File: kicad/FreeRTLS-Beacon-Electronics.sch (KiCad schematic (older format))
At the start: 28 parts, among them J1 USB_B_Micro, J2 TC2030, U1 STM32F072CBTx, U2 AZ1117IH-3.3TRG1, U3 DWM1001

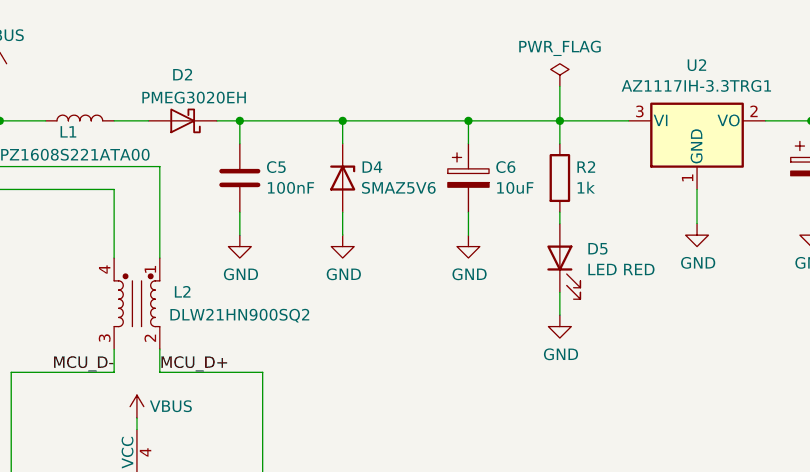
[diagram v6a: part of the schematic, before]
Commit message: Assign footprints
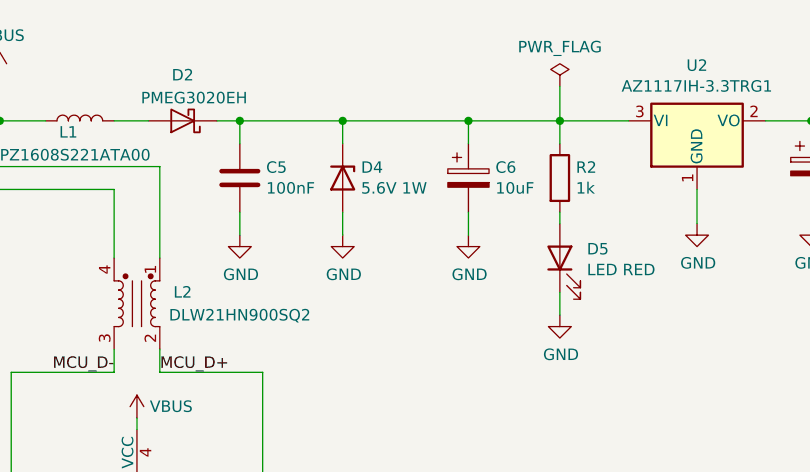
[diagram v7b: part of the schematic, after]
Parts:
- C1, C2, C3, C4, C5, C6, C7, C8, C9: footprint (none) -> Capacitor_SMD:C_0603_1608Metric
- D3: footprint (none) -> LED_SMD:LED_0603_1608Metric
- D4: value SMAZ5V6 -> 5.6V 1W; footprint (none) -> Diode_SMD:D_SOD-123; DK_Detail_Page https://www.digikey.com/en/products/detail/micro-commercial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 -> https://www.digikey.com/en/products/detail/rohm-semiconduct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; Digi-Key_PN SMAZ5V6-TPMSCT-ND -> KDZVTFTR5.6BCT-ND; MPN SMAZ5V6-TP -> KDZVTFTR5.6B; Manufacturer Micro Commercial Co -> Rohm Semiconductor
- D5: footprint (none) -> LED_SMD:LED_0603_1608Metric_Castellated
- D6: footprint (none) -> FreeRTLS-Beacon:LED_L955QEQGC-TR_3.2x2.7mm_P1.7mm
- L1, L3, L4: footprint (none) -> Inductor_SMD:L_0603_1608Metric
- L2: footprint (none) -> FreeRTLS-Beacon:FIL_DLW21HN900SQ2L
- R1, R2, R3, R5: footprint (none) -> Resistor_SMD:R_0603_1608Metric
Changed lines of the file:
@@
 F 0 "C5" H 2615 1296 50  0000 L CNN
 F 1 "100nF" H 2615 1205 50  0000 L CNN
-F 2 "" H 2538 1100 50  0001 C CNN
+F 2 "Capacitor_SMD:C_0603_1608Metric" H 2538 1100 50  0001 C CNN
 F 3 "~" H 2500 1250 50  0001 C CNN
 F 4 "https://www.digikey.com/en/products/detail/kemet/C0603C104Z3VACTU/411099" H 2500 1250 50  0001 C CNN "DK_Detail_Page"
@@
 P 2950 1250
 F 0 "D4" V 2904 1330 50  0000 L CNN
-F 1 "SMAZ5V6" V 2995 1330 50  0000 L CNN
-F 2 "" H 2950 1250 50  0001 C CNN
+F 1 "5.6V 1W" V 2995 1330 50  0000 L CNN
+F 2 "Diode_SMD:D_SOD-123" H 2950 1250 50  0001 C CNN
 F 3 "~" H 2950 1250 50  0001 C CNN
-F 4 "https://www.digikey.com/en/products/detail/micro-commercial-co/SMAZ5V6-TP/1793259" H 2950 1250 50  0001 C CNN "DK_Detail_Page"
-F 5 "SMAZ5V6-TPMSCT-ND" H 2950 1250 50  0001 C CNN "Digi-Key_PN"
-F 6 "SMAZ5V6-TP" H 2950 1250 50  0001 C CNN "MPN"
-F 7 "Micro Commercial Co" H 2950 1250 50  0001 C CNN "Manufacturer"
+F 4 "https://www.digikey.com/en/products/detail/rohm-semiconductor/KDZVTFTR5-6B/9697270" H 2950 1250 50  0001 C CNN "DK_Detail_Page"
+F 5 "KDZVTFTR5.6BCT-ND" H 2950 1250 50  0001 C CNN "Digi-Key_PN"
+F 6 "KDZVTFTR5.6B" H 2950 1250 50  0001 C CNN "MPN"
+F 7 "Rohm Semiconductor" H 2950 1250 50  0001 C CNN "Manufacturer"
 	1    2950 1250
 	0    1    1    0
@@
 F 0 "C6" H 3618 1296 50  0000 L CNN
 F 1 "10uF" H 3618 1205 50  0000 L CNN
-F 2 "" H 3538 1100 50  0001 C CNN
+F 2 "Capacitor_SMD:C_0603_1608Metric" H 3538 1100 50  0001 C CNN
 F 3 "~" H 3500 1250 50  0001 C CNN
 F 4 "https://www.digikey.com/en/products/detail/venkel/C0603X6S100-106MNP/12332839" H 3500 1250 50  0001 C CNN "DK_Detail_Page"
@@
 F 0 "R2" H 3970 1296 50  0000 L CNN
 F 1 "1k" H 3970 1205 50  0000 L CNN
-F 2 "" V 3830 1250 50  0001 C CNN
+F 2 "Resistor_SMD:R_0603_1608Metric" V 3830 1250 50  0001 C CNN
 F 3 "~" H 3900 1250 50  0001 C CNN
 F 4 "https://www.digikey.com/en/products/detail/yageo/RC0603JR-071KL/726677" H 3900 1250 50  0001 C CNN "DK_Detail_Page"
@@
 F 0 "D5" V 3939 1482 50  0000 R CNN
 F 1 "LED RED" V 3848 1482 50  0000 R CNN
-F 2 "" H 3900 1600 50  0001 C CNN
+F 2 "LED_SMD:LED_0603_1608Metric_Castellated" H 3900 1600 50  0001 C CNN
 F 3 "~" H 3900 1600 50  0001 C CNN
 F 4 "https://www.digikey.com/en/products/detail/w%C3%BCrth-elektronik/150060RS75000/4489901" H 3900 1600 50  0001 C CNN "DK_Detail_Page"
@@
 F 0 "C7" H 5118 1246 50  0000 L CNN
 F 1 "10uF" H 5118 1155 50  0000 L CNN
-F 2 "" H 5038 1050 50  0001 C CNN
+F 2 "Capacitor_SMD:C_0603_1608Metric" H 5038 1050 50  0001 C CNN
 F 3 "~" H 5000 1200 50  0001 C CNN
 F 4 "https://www.digikey.com/en/products/detail/venkel/C0603X6S100-106MNP/12332839" H 5000 1200 50  0001 C CNN "DK_Detail_Page"
@@
 F 0 "L3" V 5550 1000 50  0000 C CNN
 F 1 "MPZ1608S601ATA00" V 5350 800 50  0000 C CNN
-F 2 "" H 5450 1000 50  0001 C CNN
+F 2 "Inductor_SMD:L_0603_1608Metric" H 5450 1000 50  0001 C CNN
 F 3 "~" H 5450 1000 50  0001 C CNN
 F 4 "https://www.digikey.com/en/products/detail/tdk-corporation/MPZ1608S601ATA00/765064" H 5450 1000 50  0001 C CNN "DK_Detail_Page"
@@
 F 0 "C1" H 4450 4200 50  0000 L CNN
 F 1 "1uF" H 4450 4100 50  0000 L CNN
-F 2 "" H 4388 4000 50  0001 C CNN
+F 2 "Capacitor_SMD:C_0603_1608Metric" H 4388 4000 50  0001 C CNN
 F 3 "~" H 4350 4150 50  0001 C CNN
 F 4 "https://www.digikey.com/en/products/detail/samsung-electro-mechanics/CL10A105KP8NNNC/3886840" H 4350 4150 50  0001 C CNN "DK_Detail_Page"
@@
 F 0 "C2" H 4800 4200 50  0000 L CNN
 F 1 "100nF" H 4800 4100 50  0000 L CNN
-F 2 "" H 4738 4000 50  0001 C CNN
+F 2 "Capacitor_SMD:C_0603_1608Metric" H 4738 4000 50  0001 C CNN
 F 3 "~" H 4700 4150 50  0001 C CNN
 F 4 "https://www.digikey.com/en/products/detail/kemet/C0603C104Z3VACTU/411099" H 4700 4150 50  0001 C CNN "DK_Detail_Page"
@@
 F 0 "C3" H 5250 4200 50  0000 L CNN
 F 1 "100nF" H 5250 4100 50  0000 L CNN
-F 2 "" H 5188 4000 50  0001 C CNN
+F 2 "Capacitor_SMD:C_0603_1608Metric" H 5188 4000 50  0001 C CNN
 F 3 "~" H 5150 4150 50  0001 C CNN
 F 4 "https://www.digikey.com/en/products/detail/kemet/C0603C104Z3VACTU/411099" H 5150 4150 50  0001 C CNN "DK_Detail_Page"
@@
 F 0 "C4" H 5700 4200 50  0000 L CNN
 F 1 "100nF" H 5700 4100 50  0000 L CNN
-F 2 "" H 5638 4000 50  0001 C CNN
+F 2 "Capacitor_SMD:C_0603_1608Metric" H 5638 4000 50  0001 C CNN
 F 3 "~" H 5600 4150 50  0001 C CNN
 F 4 "https://www.digikey.com/en/products/detail/kemet/C0603C104Z3VACTU/411099" H 5600 4150 50  0001 C CNN "DK_Detail_Page"
@@
 F 0 "R1" H 2220 5246 50  0000 L CNN
 F 1 "1k" H 2220 5155 50  0000 L CNN
-F 2 "" V 2080 5200 50  0001 C CNN
+F 2 "Resistor_SMD:R_0603_1608Metric" V 2080 5200 50  0001 C CNN
 F 3 "~" H 2150 5200 50  0001 C CNN
 F 4 "https://www.digikey.com/en/products/detail/yageo/RC0603JR-071KL/726677" H 2150 5200 50  0001 C CNN "DK_Detail_Page"
@@
 F 0 "D3" V 2150 5050 50  0000 R CNN
 F 1 "LED GREEN" V 2050 5300 50  0000 R CNN
-F 2 "" H 2150 4850 50  0001 C CNN
+F 2 "LED_SMD:LED_0603_1608Metric" H 2150 4850 50  0001 C CNN
 F 3 "~" H 2150 4850 50  0001 C CNN
 F 4 "https://www.digikey.com/en/products/detail/w%C3%BCrth-elektronik/150060GS75000/4489898" H 2150 4850 50  0001 C CNN "DK_Detail_Page"
@@
 F 0 "R3" H 10170 3496 50  0000 L CNN
 F 1 "1k" H 10170 3405 50  0000 L CNN
-F 2 "" V 10030 3450 50  0001 C CNN
+F 2 "Resistor_SMD:R_0603_1608Metric" V 10030 3450 50  0001 C CNN
 F 3 "~" H 10100 3450 50  0001 C CNN
 F 4 "https://www.digikey.com/en/products/detail/yageo/RC0603JR-071KL/726677" H 10100 3450 50  0001 C CNN "DK_Detail_Page"
@@
 F 0 "R5" H 10150 3500 50  0000 L CNN
 F 1 "470" H 10100 3400 50  0000 L CNN
-F 2 "" V 10230 3450 50  0001 C CNN
+F 2 "Resistor_SMD:R_0603_1608Metric" V 10230 3450 50  0001 C CNN
 F 3 "~" H 10300 3450 50  0001 C CNN
 F 4 "https://www.digikey.com/en/products/detail/yageo/RC0603JR-07470RL/726791" H 10300 3450 50  0001 C CNN "DK_Detail_Page"
@@
 F 0 "C9" H 7568 2646 50  0000 L CNN
 F 1 "100nF" H 7568 2555 50  0000 L CNN
-F 2 "" H 7488 2450 50  0001 C CNN
+F 2 "Capacitor_SMD:C_0603_1608Metric" H 7488 2450 50  0001 C CNN
 F 3 "~" H 7450 2600 50  0001 C CNN
 F 4 "https://www.digikey.com/en/products/detail/kemet/C0603C104Z3VACTU/411099" H 7450 2600 50  0001 C CNN "DK_Detail_Page"
@@
 F 0 "C8" H 7165 2646 50  0000 L CNN
 F 1 "10uF" H 7165 2555 50  0000 L CNN
-F 2 "" H 7088 2450 50  0001 C CNN
+F 2 "Capacitor_SMD:C_0603_1608Metric" H 7088 2450 50  0001 C CNN
 F 3 "~" H 7050 2600 50  0001 C CNN
 F 4 "https://www.digikey.com/en/products/detail/venkel/C0603X6S100-106MNP/12332839" H 7050 2600 50  0001 C CNN "DK_Detail_Page"
@@
 F 0 "L4" V 950 2000 50  0000 C CNN
 F 1 "MPZ1608S221ATA00" V 850 2000 50  0000 C CNN
-F 2 "" H 1000 1850 50  0001 C CNN
+F 2 "Inductor_SMD:L_0603_1608Metric" H 1000 1850 50  0001 C CNN
 F 3 "~" H 1000 1850 50  0001 C CNN
 F 4 "https://www.digikey.com/en/products/detail/tdk-corporation/MPZ1608S221ATA00/571872" H 1000 1850 50  0001 C CNN "DK_Detail_Page"
@@
 F 0 "L2" V 2000 2000 50  0000 C CNN
 F 1 "DLW21HN900SQ2" V 2100 2250 50  0000 C CNN
-F 2 "" H 2050 1800 50  0001 C CNN
+F 2 "FreeRTLS-Beacon:FIL_DLW21HN900SQ2L" H 2050 1800 50  0001 C CNN
 F 3 "https://www.murata.com/products/productdata/8796757491742/EFLC0005.pdf?1544104809000" H 2050 1800 50  0001 C CNN
 F 4 "https://www.digikey.com/en/products/detail/murata-electronics/DLW21HN900SQ2L/584273" H 2050 1800 50  0001 C CNN "DK_Detail_Page"
@@
 F 0 "L1" V 1750 1050 50  0000 C CNN
 F 1 "MPZ1608S221ATA00" V 1650 1050 50  0000 C CNN
-F 2 "" H 1800 1000 50  0001 C CNN
+F 2 "Inductor_SMD:L_0603_1608Metric" H 1800 1000 50  0001 C CNN
 F 3 "~" H 1800 1000 50  0001 C CNN
 F 4 "https://www.digikey.com/en/products/detail/tdk-corporation/MPZ1608S221ATA00/571872" H 1800 1000 50  0001 C CNN "DK_Detail_Page"
@@
 F 0 "D6" V 10246 3740 50  0000 R CNN
 F 1 "L955QEQGC-TR" V 10155 3740 50  0000 R CNN
-F 2 "" H 10230 3950 50  0001 C CNN
+F 2 "FreeRTLS-Beacon:LED_L955QEQGC-TR_3.2x2.7mm_P1.7mm" H 10230 3950 50  0001 C CNN
 F 3 "https://www.aopled.com/AOP_PDFs/L955QEQGC-TR.pdf" H 10230 3950 50  0001 C CNN
 F 4 "https://www.digikey.com/en/products/detail/american-opto-plus-led/L955QEQGC-TR/13243458" H 10200 3950 50  0001 C CNN "DK_Detail_Page"

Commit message: Remove ü and add .DS_Store to gitignore
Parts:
- D3, D5: Manufacturer Würth Elektronik -> Wurth Elektronik
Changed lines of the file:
@@
 F 5 "732-4978-1-ND" H 3900 1600 50  0001 C CNN "Digi-Key_PN"
 F 6 "150060RS75000" H 3900 1600 50  0001 C CNN "MPN"
-F 7 "Würth Elektronik" H 3900 1600 50  0001 C CNN "Manufacturer"
+F 7 "Wurth Elektronik" H 3900 1600 50  0001 C CNN "Manufacturer"
 	1    3900 1600
 	0    -1   -1   0
@@
 F 5 "732-4971-1-ND" H 2150 4850 50  0001 C CNN "Digi-Key_PN"
 F 6 "150060GS75000" H 2150 4850 50  0001 C CNN "MPN"
-F 7 "Würth Elektronik" H 2150 4850 50  0001 C CNN "Manufacturer"
+F 7 "Wurth Elektronik" H 2150 4850 50  0001 C CNN "Manufacturer"
 	1    2150 4850
 	0    -1   -1   0
